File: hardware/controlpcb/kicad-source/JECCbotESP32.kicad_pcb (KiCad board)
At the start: 2 copper layers, 100 x 100 mm, 164 parts, among them CN1 691322310002, CN2 691322310004, CN3 691322310004, CN4 691322310004, CN5 691322310004, CON1 Micro_SDCard, P1 WR-TBL_691313710002, P2 WR-TBL_691313710002, P3 WR-TBL_691313710002, P4 WR-TBL_691313710002, P5 USB_OTG, P6 CONN_01X08, P7 CONN_02X10, P8 CONN_01X03, Q1 IPD90P03P4L- 04, Q2 BC847, Q3 BC847, Q4 2N7002, SW1 TAST_VER, SW2 TAST_VER, U1 ESP32_WROOM_32, U10 IFX007T, U11 OPA2374AIDCN, U12 IFX007T, U13 IFX007T, U14 74xx08, U15 74xx08, U16 IFX007T, U17 CP2102N_28, U2 74xx4052, U3 74xx4052, U4 TCA9534, U5 ADS1015, U6 IFX91041EFJ, U7 LM317, U8 OPA2374AIDCN, U9 IFX007T

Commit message: added rendering and schematics pdf
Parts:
- moved P8 2.03 mm to (52.5, 110.4)
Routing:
- net GPIO5: track 103.8 -> 101.1 mm
- net +5V: track 194.6 -> 192.6 mm
- net SCK: track 112.4 -> 113.5 mm
- net GND: vias 249 -> 272

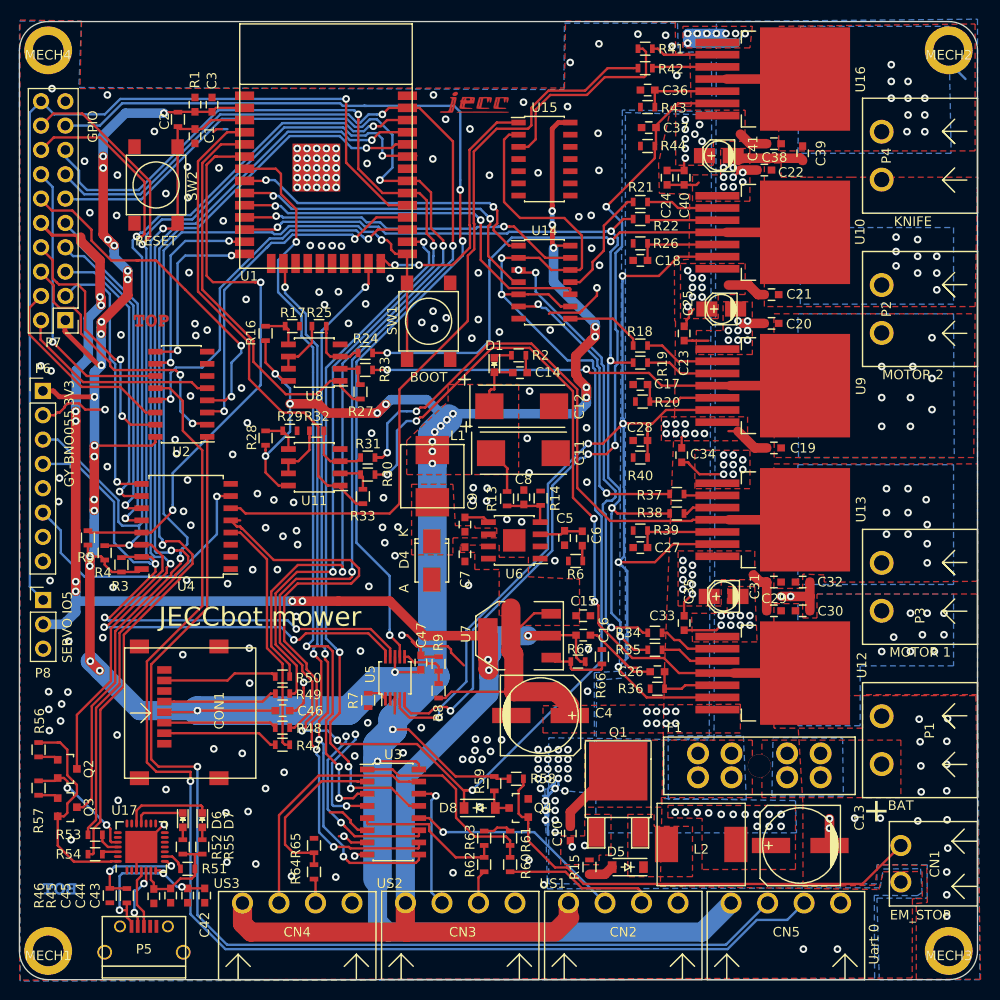
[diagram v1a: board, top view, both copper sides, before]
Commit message: added servo connector
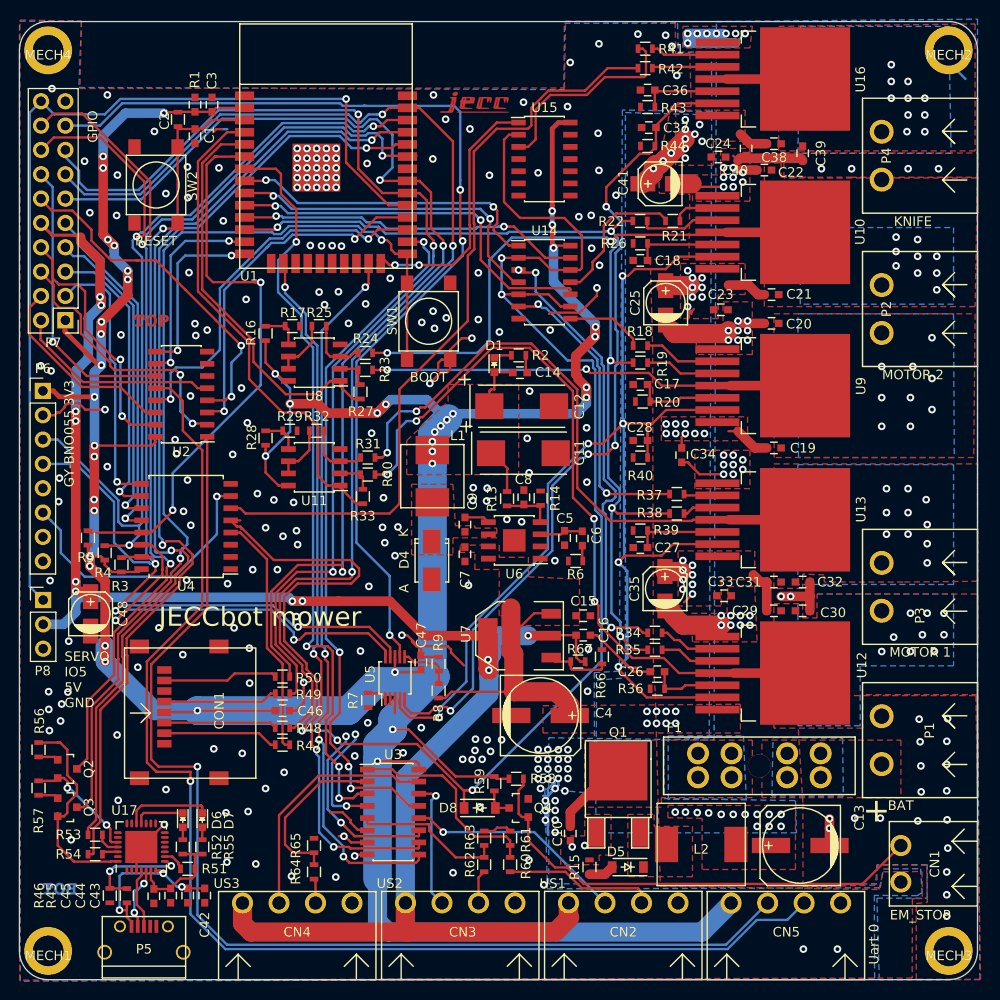
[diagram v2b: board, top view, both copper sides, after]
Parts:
- added C48: DNI, capacitors:c_elec_4x4.5, F.Cu at (57.4, 111.8)
- C25, C35, C41: footprint capacitors:c_elec_3x5.3 -> capacitors:c_elec_4x4.5
- moved C40 7.15 mm to (125.8, 63.2)
- moved C41 6.79 mm to (116.9, 66.9)
- moved C35 6.17 mm to (117.4, 109.2), turned to 90 degrees
- moved C25 5.84 mm to (117.5, 79.4), turned to 90 degrees
- moved C24 5.77 mm to (123.0, 64.1), turned to 0 degrees
- moved C33 5.05 mm to (123.5, 109.9), turned to 0 degrees
- moved C23 4.56 mm to (123.2, 80.1), turned to 0 degrees
- moved R21 3.92 mm to (118.2, 70.8)
- moved R22 0.20 mm to (114.8, 70.8)
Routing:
- net GND: track 130.9 -> 151.2 mm, vias 272 -> 279
- net +BATT: track 57.8 -> 67.7 mm, vias 53 -> 56
- net /POWERTRAIN/IN4: track 12.0 -> 15.3 mm
- net Net-(R21-Pad1): track 7.55 -> 4.88 mm
- net +5V: track 192.6 -> 194.8 mm
- net SDA: track 154.9 -> 153.1 mm
- net +3V3: track 383.6 -> 382.4 mm
- net Net-(R22-Pad1): track 7.34 -> 8.41 mm
- net SCL: track 151.7 -> 150.9 mm
- net KNIFE_IS: track 86.6 -> 87.2 mm
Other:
- board text added: "SERVO IO5 5V GND"
- board text removed: "SERVO IO5"

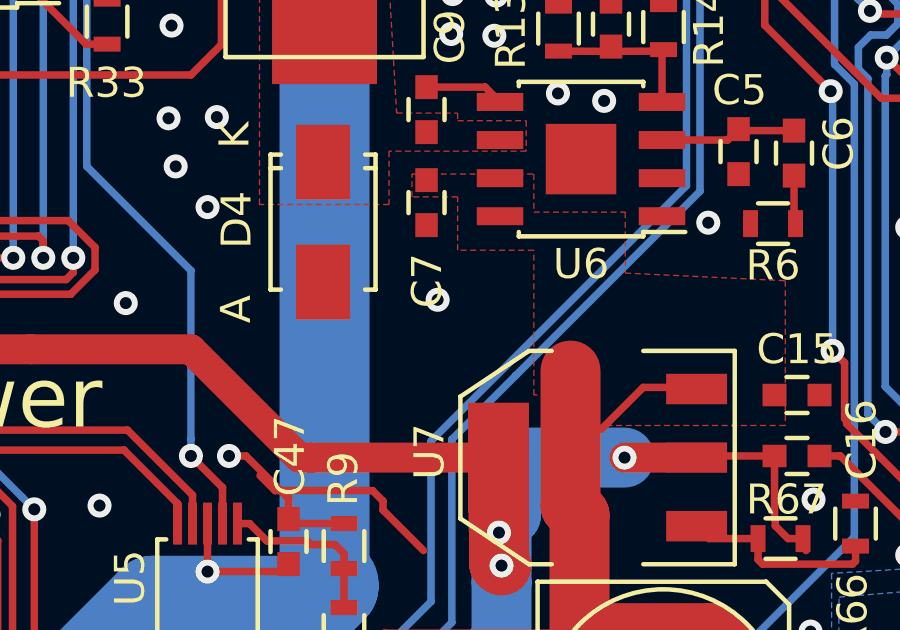
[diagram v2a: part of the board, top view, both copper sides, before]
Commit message: changed layout
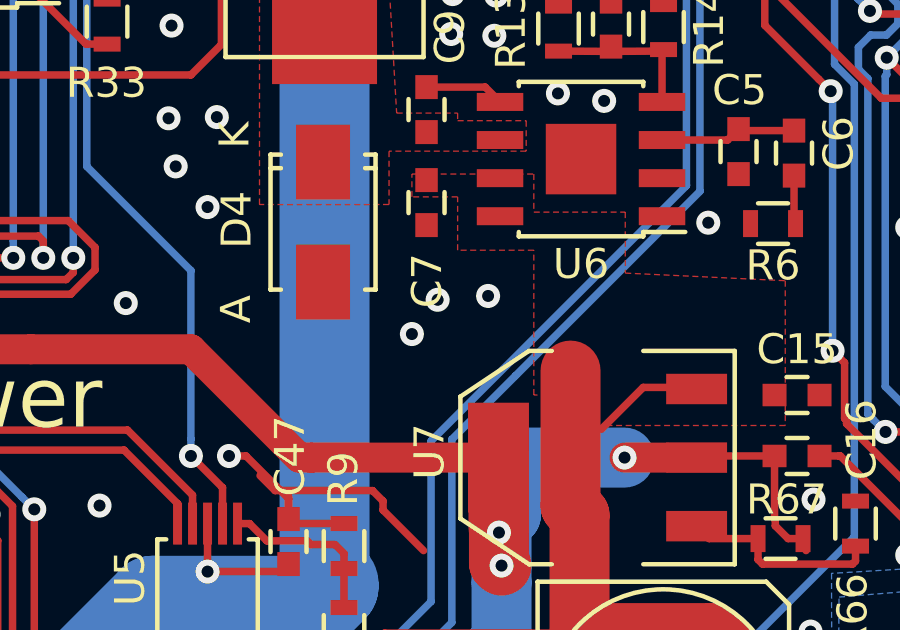
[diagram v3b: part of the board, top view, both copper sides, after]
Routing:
- net GND: vias 279 -> 281
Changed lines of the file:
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@@
     (thickness 1.6)
     (drawings 29)
-    (tracks 2456)
+    (tracks 2458)
     (zones 0)
     (modules 165)
@@
   (via (at 142.76 65.36) (size 0.8) (drill 0.4) (layers F.Cu B.Cu) (net 1))
   (via (at 145.93 65.36) (size 0.8) (drill 0.4) (layers F.Cu B.Cu) (net 1))
+  (via (at 96.012 109.982) (size 0.8) (drill 0.4) (layers F.Cu B.Cu) (net 1))
+  (via (at 98.552 108.712) (size 0.8) (drill 0.4) (layers F.Cu B.Cu) (net 1))
   (via (at 95.25 90.932) (size 0.8) (drill 0.4) (layers F.Cu B.Cu) (net 2))
   (segment (start 94.107 92.075) (end 94.742 91.44) (width 3) (layer B.Cu) (net 2))

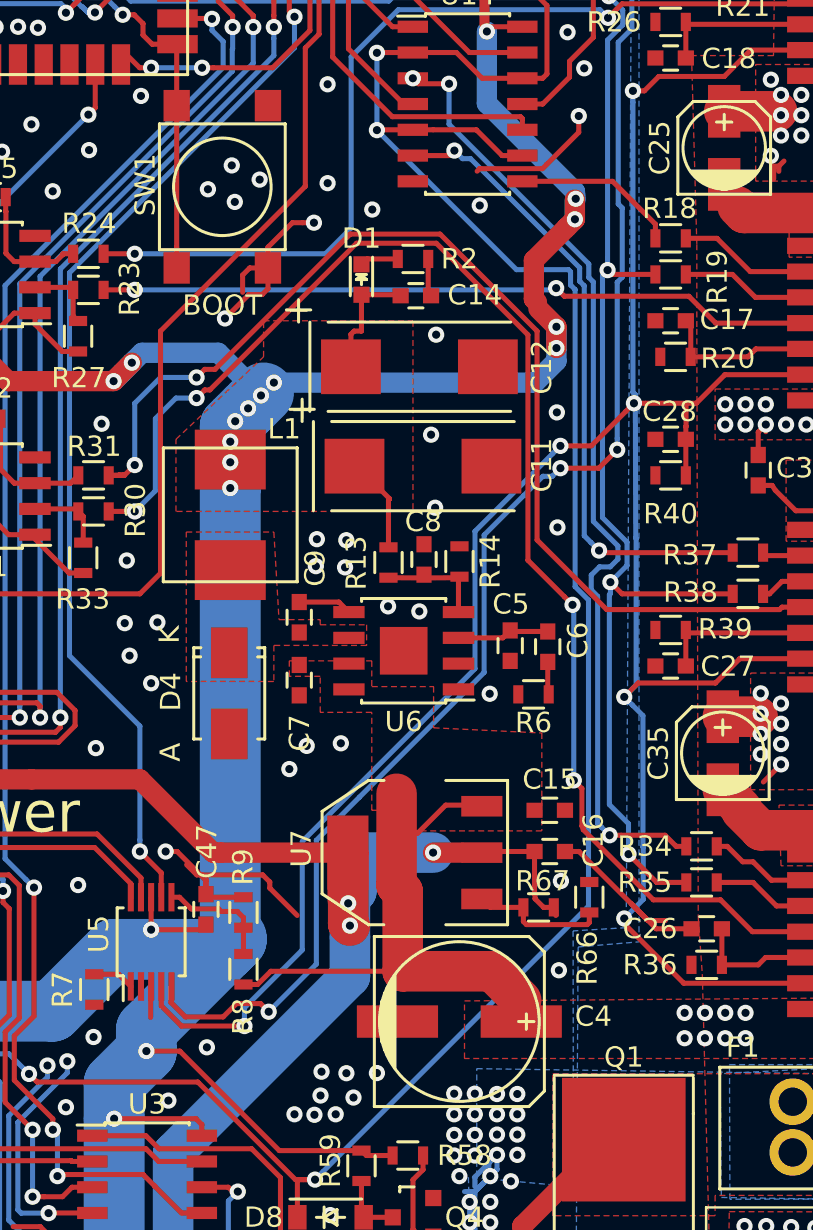
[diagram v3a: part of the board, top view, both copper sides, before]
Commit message: changed power supply
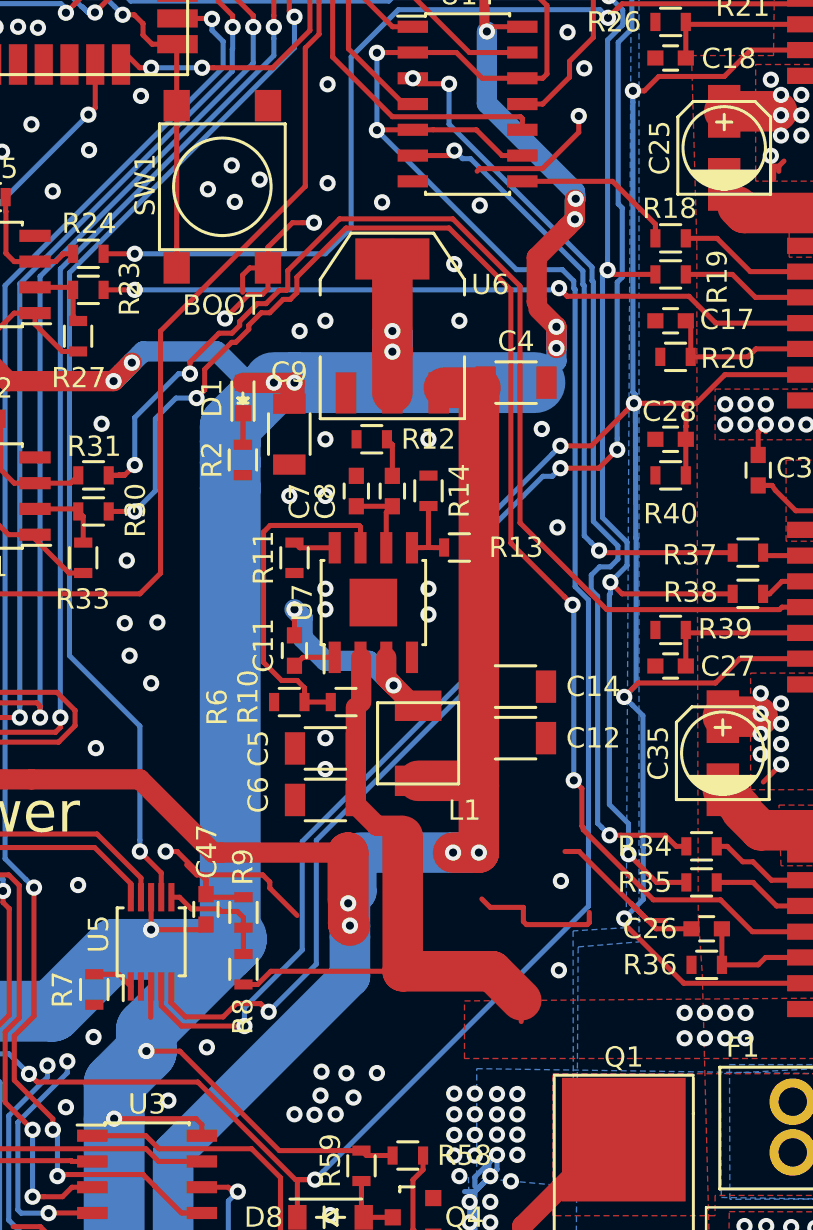
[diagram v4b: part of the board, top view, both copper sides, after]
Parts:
- removed C15: 10u, capacitors:C_0603
- removed C16: 22u, capacitors:C_0603
- removed D4: SSA34, diodes:SMA_Standard
- removed R66: 720, resistors:R_0603
- removed R67: 240, resistors:R_0603
- added R10: 43.2k, resistors:R_0603, F.Cu at (96.0, 106.7)
- added R11: 143k, resistors:R_0603, F.Cu at (96.3, 99.6)
- added R12: 3.74k, resistors:R_0603, F.Cu at (100.1, 93.7)
- C11: value 330uF 6.3V -> 100nF; footprint capacitors:TantalC_SizeD_EIA-7343_Wave -> capacitors:C_0603
- C12: value 330uF 6.3V -> 22uF; footprint capacitors:TantalC_SizeD_EIA-7343_Wave -> capacitors:C_1206
- C14: value 100nF -> 22uF; footprint capacitors:C_0603 -> capacitors:C_1206
- C4: value 47uF 50V -> 10uF; footprint capacitors:c_elec_8x6.7 -> capacitors:C_1206
- C5: value DNI -> 4.7uF 50V; footprint capacitors:C_0603 -> capacitors:C_1206
- C6: value 22nF -> 4.7uF 50V; footprint capacitors:C_0603 -> capacitors:C_1206
- C7: value 100nF -> 120pF
- C8: value 470pF -> 12nF
- C9: value 220nF -> 22uF; footprint capacitors:C_0603 -> capacitors:C_1206
- L1: value 74437346220 -> 74437324150; footprint L_power:WE-LHMI70xx -> L_power:WE-LHMI40xx
- R13: value 10k -> 100k
- R14: value 2k2 -> 19.1k
- R6: value 22k -> 220k
- U6: value IFX91041EFJ -> LT1117; footprint SOIC:SOIC-8-1EP_3.9x4.9mm_Pitch1.27mm -> SOT_TO:SOT-223
- U7: value LM317 -> TPS54335A; footprint SOT_TO:SOT-223 -> SOIC:SOIC-8-1EP_3.9x4.9mm_Pitch1.27mm
- moved C4 31.6 mm to (107.2, 90.9)
- moved C14 19.9 mm to (107.2, 105.9)
- moved C12 18.9 mm to (107.2, 108.5)
- moved U6 16.0 mm to (101.1, 88.1), turned to 0 degrees
- moved L1 14.6 mm to (102.4, 108.7), turned to 270 degrees
- moved C6 13.3 mm to (97.8, 111.5), turned to 180 degrees
- moved R2 13.0 mm to (93.7, 94.7), turned to 270 degrees
- moved U7 12.5 mm to (100.2, 101.8)
- moved C11 11.1 mm to (96.3, 104.1), turned to 270 degrees
- moved C5 10.4 mm to (97.8, 109.0), turned to 180 degrees
- moved C7 9.74 mm to (99.3, 96.3), turned to 90 degrees
- moved R6 9.25 mm to (98.8, 106.7)
- moved C9 9.04 mm to (96.0, 93.5)
- moved D1 8.26 mm to (93.7, 91.7), turned to 90 degrees
- moved R14 3.81 mm to (102.9, 96.3)
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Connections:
- C11 pad 1: +3V3 -> /POWER/PH
- C11 pad 2: GND -> Net-(C11-Pad2)
- C12 pad 1: +3V3 -> +5V
- C14 pad 1: +3V3 -> +5V
- C4 pad 1: +BATT -> +5V
- C5 pad 1: /POWER/COMP -> +BATT
- C6 pad 1: /POWER/COMP -> +BATT
- C6 pad 2: Net-(C6-Pad2) -> GND
- C7 pad 1: +BATT -> /POWER/COMP
- C8 pad 1: /POWER/FB -> /POWER/COMP
- C8 pad 2: GND -> Net-(C8-Pad2)
- C9 pad 1: /POWER/BDS -> +3V3
- C9 pad 2: /POWER/BUO -> GND
- L1 pad 1: /POWER/BUO -> /POWER/PH
- L1 pad 2: +3V3 -> +5V
- R13 pad 1: +3V3 -> +5V
- R13 pad 2: /POWER/FB -> /POWER/SENSE5V
- R14 pad 1: /POWER/FB -> /POWER/SENSE5V
- R6 pad 1: Net-(C6-Pad2) -> +BATT
- R6 pad 2: GND -> /POWER/EN
- U6 pad 2: GND -> +3V3
- U6 pad 3: /POWER/COMP -> +5V
- U6 pad 4: /POWER/FB -> +3V3
- U7 pad 1: Net-(R66-Pad1) -> Net-(C11-Pad2)
- U7 pad 2: +5V -> +BATT
- U7 pad 3: +BATT -> /POWER/PH
- U7 pad 4: +5V -> GND
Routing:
- net +5V: track 194.8 -> 217.6 mm, vias 11 -> 12
- net /POWER/EN: track 0.00 -> 16.9 mm
- net /POWER/PH: track 0.00 -> 11.5 mm, vias 0 -> 2
- net /POWER/FB: track 5.39 -> 0.00 mm
- net /POWER/SENSE5V: track 0.00 -> 3.63 mm
- net +3V3: track 382.4 -> 385.6 mm, vias 42 -> 39
- net +BATT: track 67.7 -> 70.8 mm
- net /POWER/BDS: track 2.66 -> 0.00 mm
- net /POWERTRAIN/OUT_A1: track 79.2 -> 81.8 mm
- net Net-(C11-Pad2): track 0.00 -> 2.16 mm
- net /POWER/RT: track 0.00 -> 2.09 mm
- net /POWERTRAIN/OUT_A2: track 65.8 -> 67.8 mm
- net Net-(C8-Pad2): track 0.00 -> 1.91 mm
- net GND: track 151.2 -> 149.4 mm, vias 281 -> 282
- net Net-(C6-Pad2): track 1.62 -> 0.00 mm
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- removed copper zone on F.Cu, net +3V3
- removed copper zone on F.Cu, net /POWER/BUO

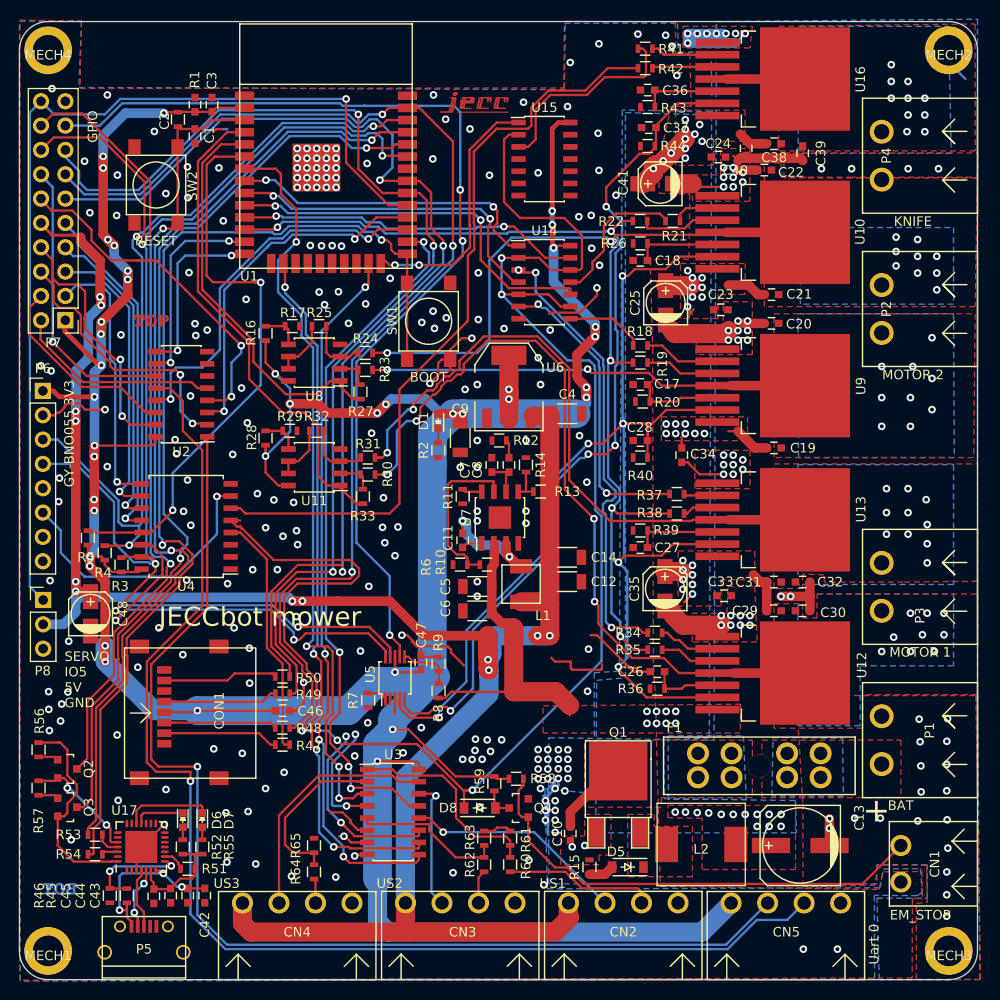
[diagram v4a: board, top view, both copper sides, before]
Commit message: changed ground plane
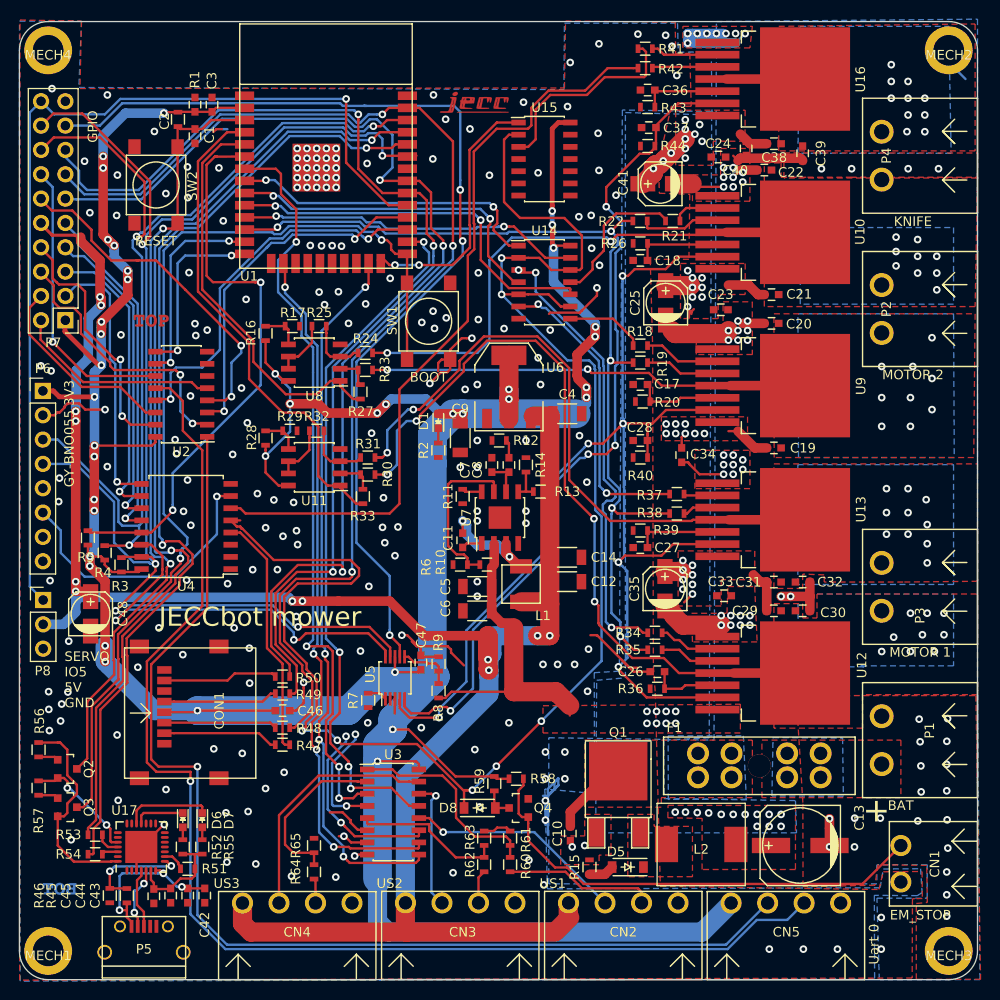
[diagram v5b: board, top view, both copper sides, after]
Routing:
- net Net-(R66-Pad1): track 6.77 -> 0.00 mm
- net /POWERTRAIN/OUT_A1: track 81.8 -> 81.2 mm
- net GND: vias 282 -> 261
- net EM_STOP: vias 5 -> 7

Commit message: finally
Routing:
- net GND: track 149.4 -> 154.1 mm, vias 261 -> 262
- net +3V3: track 385.6 -> 387.7 mm
